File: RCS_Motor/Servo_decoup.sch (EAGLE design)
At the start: 4 parts, among them M1 SMALL_SERVO

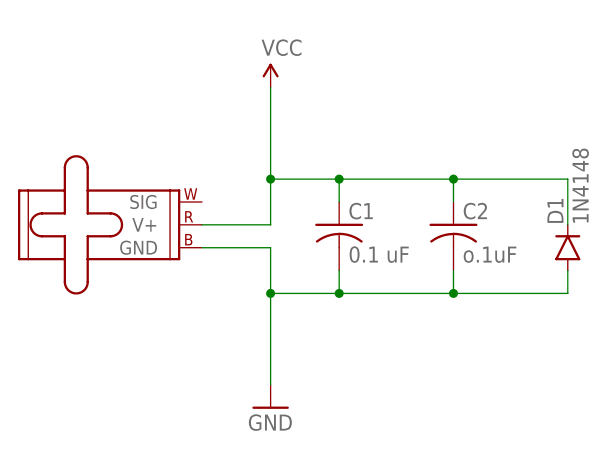
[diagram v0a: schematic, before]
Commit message: Updated/New Schematics
I don't think this updated when I did it on tuesday
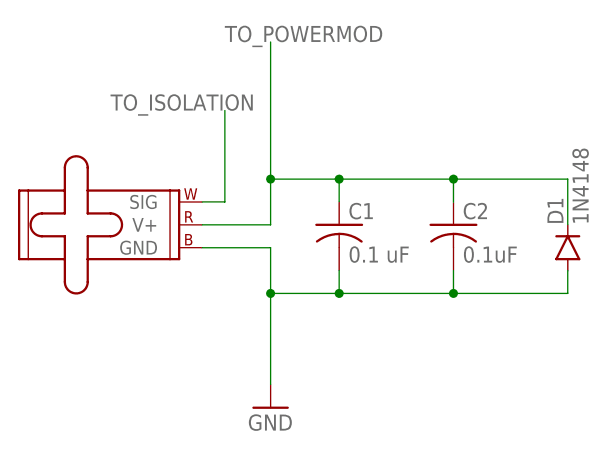
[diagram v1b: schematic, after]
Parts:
- C2: value o.1uF -> 0.1uF
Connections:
- net VCC renamed TO_POWERMOD
- new net TO_ISOLATION: M1.SIG
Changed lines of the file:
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@@
 <part name="M1" library="SparkFun-Electromechanical" deviceset="SMALL_SERVO" device=""/>
 <part name="C1" library="adafruit" deviceset="C-US" device="025-025X050" value="0.1 uF"/>
-<part name="C2" library="adafruit" deviceset="C-US" device="025-025X050" value="o.1uF"/>
+<part name="C2" library="adafruit" deviceset="C-US" device="025-025X050" value="0.1uF"/>
 <part name="GND1" library="SparkFun-Aesthetics" deviceset="GND" device=""/>
-<part name="SUPPLY1" library="SparkFun-Aesthetics" deviceset="VCC" device=""/>
 <part name="D1" library="SparkFun-DiscreteSemi" deviceset="DIODE" device="1N4148" value="1N4148"/>
 </parts>
@@
 <instance part="C2" gate="G$1" x="35.56" y="66.04"/>
 <instance part="GND1" gate="1" x="15.24" y="45.72"/>
-<instance part="SUPPLY1" gate="G$1" x="15.24" y="81.28"/>
 <instance part="D1" gate="G$1" x="48.26" y="63.5" rot="R90"/>
 </instances>
@@
 </busses>
 <nets>
-<net name="VCC" class="0">
-<segment>
-<pinref part="M1" gate="G$1" pin="V+"/>
-<pinref part="SUPPLY1" gate="G$1" pin="VCC"/>
-<wire x1="7.62" y1="66.04" x2="15.24" y2="66.04" width="0.1524" layer="91"/>
-<wire x1="15.24" y1="66.04" x2="15.24" y2="71.12" width="0.1524" layer="91"/>
-<pinref part="C2" gate="G$1" pin="1"/>
-<wire x1="15.24" y1="71.12" x2="15.24" y2="81.28" width="0.1524" layer="91"/>
-<wire x1="35.56" y1="68.58" x2="35.56" y2="71.12" width="0.1524" layer="91"/>
-<wire x1="35.56" y1="71.12" x2="22.86" y2="71.12" width="0.1524" layer="91"/>
-<pinref part="C1" gate="G$1" pin="1"/>
-<wire x1="15.24" y1="71.12" x2="22.86" y2="71.12" width="0.1524" layer="91"/>
-<wire x1="22.86" y1="71.12" x2="22.86" y2="68.58" width="0.1524" layer="91"/>
-<junction x="15.24" y="71.12"/>
-<junction x="22.86" y="71.12"/>
-<pinref part="D1" gate="G$1" pin="C"/>
-<wire x1="48.26" y1="66.04" x2="48.26" y2="71.12" width="0.1524" layer="91"/>
-<wire x1="48.26" y1="71.12" x2="35.56" y2="71.12" width="0.1524" layer="91"/>
-<junction x="35.56" y="71.12"/>
-</segment>
-</net>
 <net name="GND" class="0">
 <segment>
@@
 </segment>
 </net>
+<net name="TO_ISOLATION" class="0">
+<segment>
+<pinref part="M1" gate="G$1" pin="SIG"/>
+<wire x1="7.62" y1="68.58" x2="10.16" y2="68.58" width="0.1524" layer="91"/>
+<wire x1="10.16" y1="68.58" x2="10.16" y2="78.74" width="0.1524" layer="91"/>
+<label x="-2.54" y="78.74" size="1.778" layer="95"/>
+</segment>
+</net>
+<net name="TO_POWERMOD" class="0">
+<segment>
+<pinref part="M1" gate="G$1" pin="V+"/>
+<wire x1="7.62" y1="66.04" x2="15.24" y2="66.04" width="0.1524" layer="91"/>
+<wire x1="15.24" y1="66.04" x2="15.24" y2="71.12" width="0.1524" layer="91"/>
+<pinref part="C2" gate="G$1" pin="1"/>
+<wire x1="15.24" y1="71.12" x2="15.24" y2="86.36" width="0.1524" layer="91"/>
+<wire x1="35.56" y1="68.58" x2="35.56" y2="71.12" width="0.1524" layer="91"/>
+<wire x1="35.56" y1="71.12" x2="22.86" y2="71.12" width="0.1524" layer="91"/>
+<pinref part="C1" gate="G$1" pin="1"/>
+<wire x1="15.24" y1="71.12" x2="22.86" y2="71.12" width="0.1524" layer="91"/>
+<wire x1="22.86" y1="71.12" x2="22.86" y2="68.58" width="0.1524" layer="91"/>
+<junction x="15.24" y="71.12"/>
+<junction x="22.86" y="71.12"/>
+<pinref part="D1" gate="G$1" pin="C"/>
+<wire x1="48.26" y1="66.04" x2="48.26" y2="71.12" width="0.1524" layer="91"/>
+<wire x1="48.26" y1="71.12" x2="35.56" y2="71.12" width="0.1524" layer="91"/>
+<junction x="35.56" y="71.12"/>
+<label x="10.16" y="86.36" size="1.778" layer="95"/>
+</segment>
+</net>
